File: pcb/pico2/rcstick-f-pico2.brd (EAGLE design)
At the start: 15.4 x 28.8 mm, 43 parts, among them J1 USB-TYPEC-1054440001-HS, J2 2212S, SW1 SKRPACE010, U1 STM32F042K6U6, U2 CC2500, U3 MCP1703AT-3302E/CB, X1 16MHz/10pF, X2 26MHz/9pF, X3 (50 Ohm)

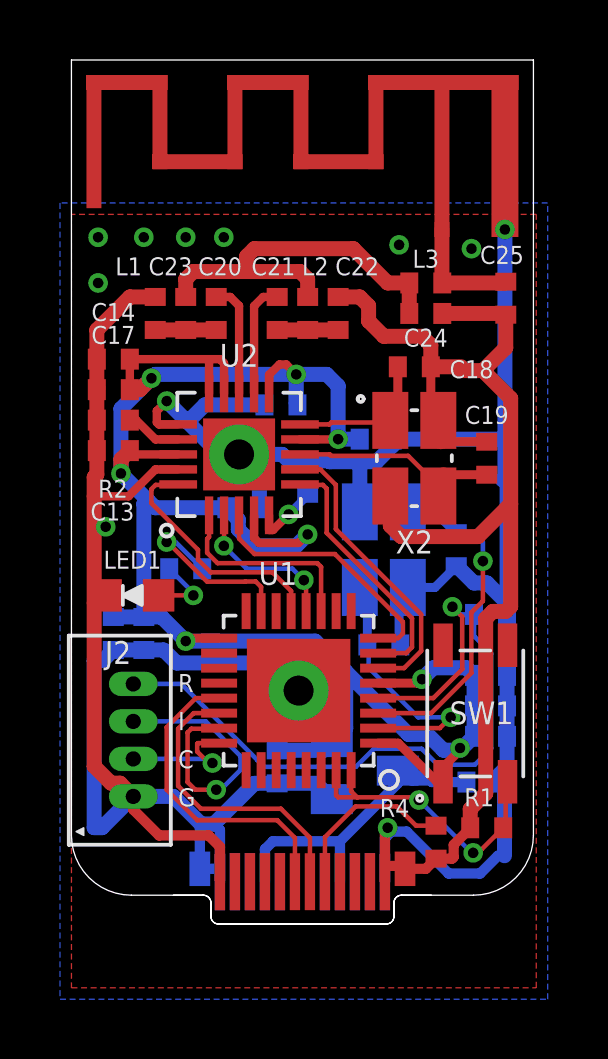
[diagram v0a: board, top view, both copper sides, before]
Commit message: added QFN28 MCU version
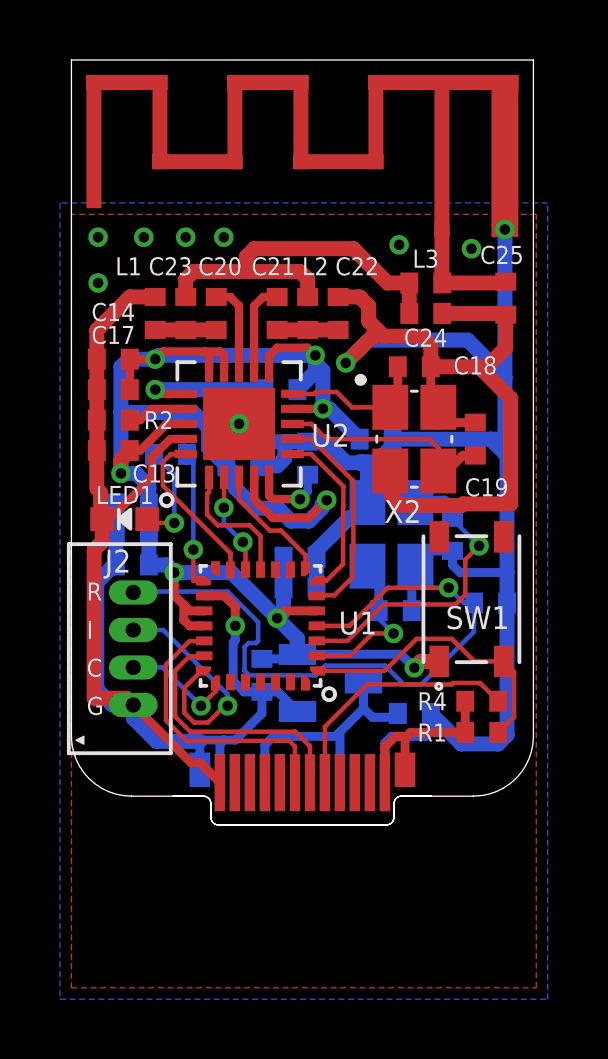
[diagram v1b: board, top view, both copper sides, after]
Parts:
- LED1: device gen-discrete:LED1608 -> gen-discrete:LED1608NONHS
- SW1: value SKRPACE010 -> SKRPACE010NONHS; device SKRPACE010:SMT(4.2X3.2) -> SKRPACE010:SMT(4.2X3.2)_ORG
- U1: value STM32F042K6U6 -> STM32F042G6U6; device stm32:UQFPN32-M -> stm32:UFQFPN28
- U2: device CC2500:CC2500-RTY1_CC2500-HS -> CC2500:CC2500-RTY1_CC2500
- U3: device SOT23_Module:SOT23 -> SOT23_Module:SOT23_NOHS
- X1, X2: device CRYSTAL3225:CRYSTAL3225-HS -> CRYSTAL3225:CRYSTAL3225
- moved C3 13.2 mm to (2.03, 14.0), turned to 0 degrees
- moved C8 7.47 mm to (7.62, 13.2)
- moved C9 7.47 mm to (7.62, 14.2)
- moved R4 4.94 mm to (13.7, 9.43), turned to 0 degrees
- moved C5 4.36 mm to (2.03, 16.0), turned to 0 degrees
- moved R3 3.84 mm to (3.30, 17.7)
- moved SW1 3.81 mm to (13.3, 12.8)
- moved C4 3.32 mm to (2.03, 15.0), turned to 0 degrees
- moved J1 3.30 mm to (7.70, 7.30)
- moved C1 3.23 mm to (11.4, 9.02)
- moved R1 3.18 mm to (13.7, 8.38)
- moved U3 3.14 mm to (8.64, 10.0)
- moved C2 3.09 mm to (6.35, 10.3)
- moved J2 3.05 mm to (2.06, 11.2)
- moved LED1 2.55 mm to (1.78, 15.5)
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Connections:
- net +3V3: now also U1.18; no longer U1.1
- net BOOT0: now also U1.1; no longer U1.31, U1.32
- net GND: now also U1.16; no longer U1.VSS, U1.VSSH
- net SWCLK: now also U1.22; no longer U1.24
- net SWDIO: now also U1.21; no longer U1.23
- net USB_D+: now also U1.20; no longer U1.22
- net USB_D-: now also U1.19; no longer U1.21
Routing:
- net GND: track 154.3 -> 137.9 mm
- net +3V3: track 70.2 -> 63.3 mm
- net RF_INT: track 8.66 -> 4.11 mm
- net OSC_IN: track 8.78 -> 5.68 mm
- net RF_TEST: track 8.62 -> 5.75 mm
- net SPI_MOSI: track 8.16 -> 5.39 mm
- net CC: track 5.88 -> 8.50 mm
- net RF_CS: track 9.80 -> 7.28 mm
- net NRST: track 24.7 -> 22.3 mm
- net SPI_SCK: track 6.74 -> 4.46 mm
- net +5V: track 11.1 -> 9.15 mm
- net SPI_MISO: track 5.23 -> 3.38 mm
- net LED: track 6.43 -> 4.86 mm
- net SWDIO: track 9.42 -> 7.86 mm
- net N$1: track 2.52 -> 3.61 mm
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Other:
- board size 15.4 x 28.8 mm -> 15.4 x 25.5 mm
- board text added: "V3.0"
- board text removed: "V2.0"
